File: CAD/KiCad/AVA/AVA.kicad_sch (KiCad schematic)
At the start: 9 parts, among them J1 Conn_01x40_Pin, J2 Barrel_Jack, M1 Motor_Servo, M2 Steering_Front_Servo, M3 Steering_Back_Servo, M4 Fan, SW1 SW_Push

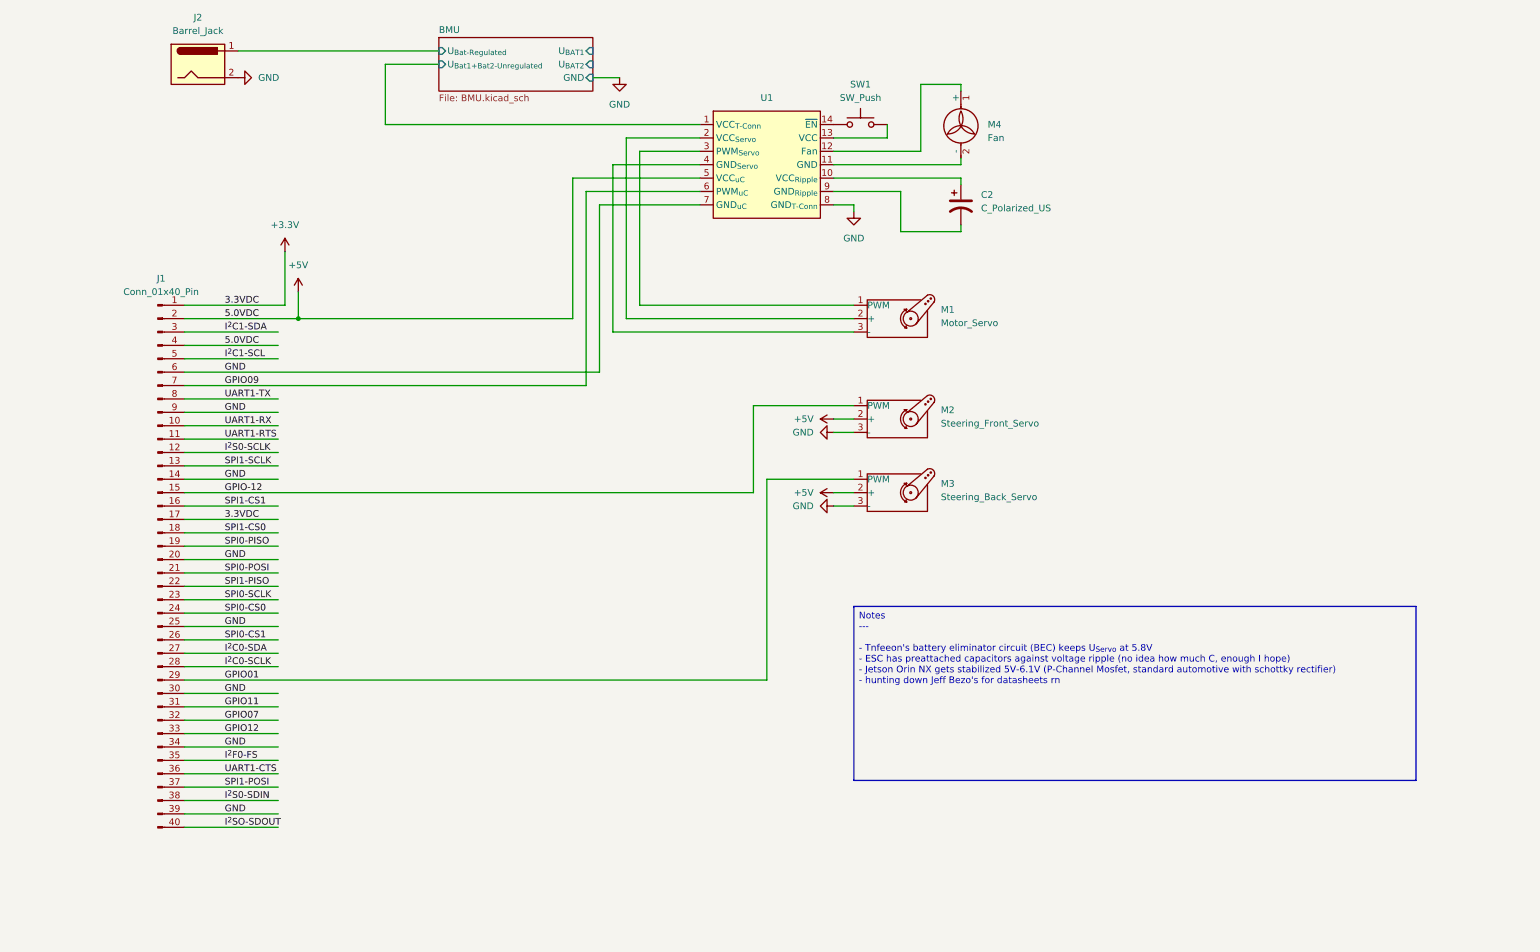
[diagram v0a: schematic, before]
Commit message: Added Graphos MBSE json file necessary for model
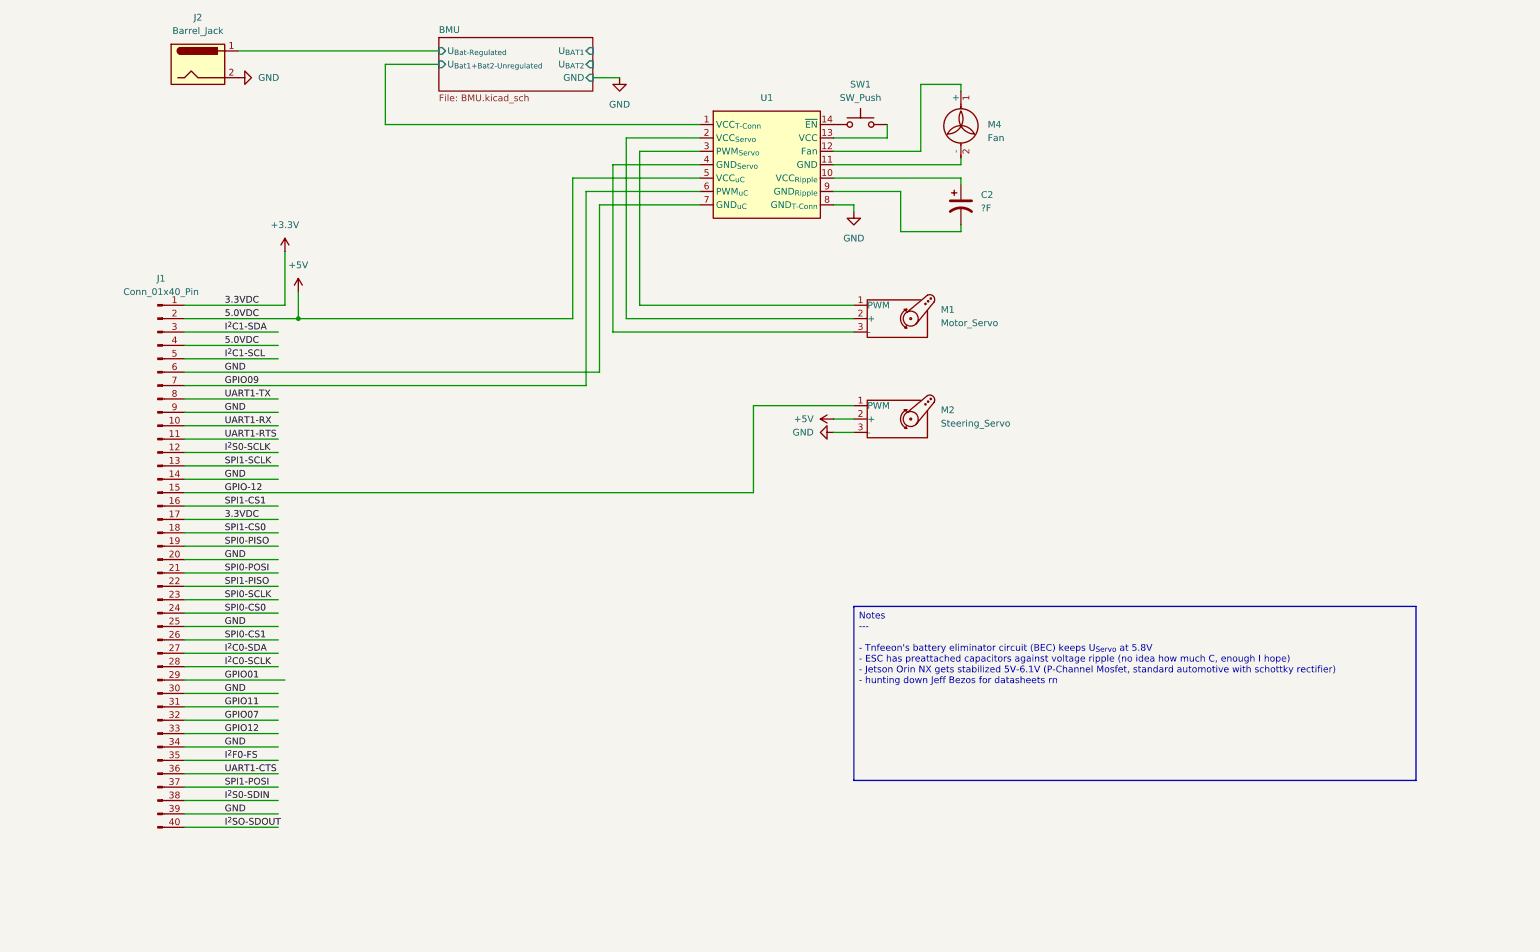
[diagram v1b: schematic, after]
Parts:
- removed M3: Steering_Back_Servo, Connector_PinHeader_2.54mm:PinHeader_1x03_P2.54mm_Vertical, symbol Motor:Motor_Servo
- C2: value C_Polarized_US -> ?F
- M2: value Steering_Front_Servo -> Steering_Servo

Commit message: ESP32-Nano for Wifi comms, ESP32-C3 for Hall Interrupt handling and BAT0, BAT1 voltage monitoring and wiring between ESC, servo and fan will be handlded on separate PCB for easier wiring. This schematic will contain this PCB, schematic and production data for it. Will probably be etched by some annoying dipshit (Meeeeeee :3)
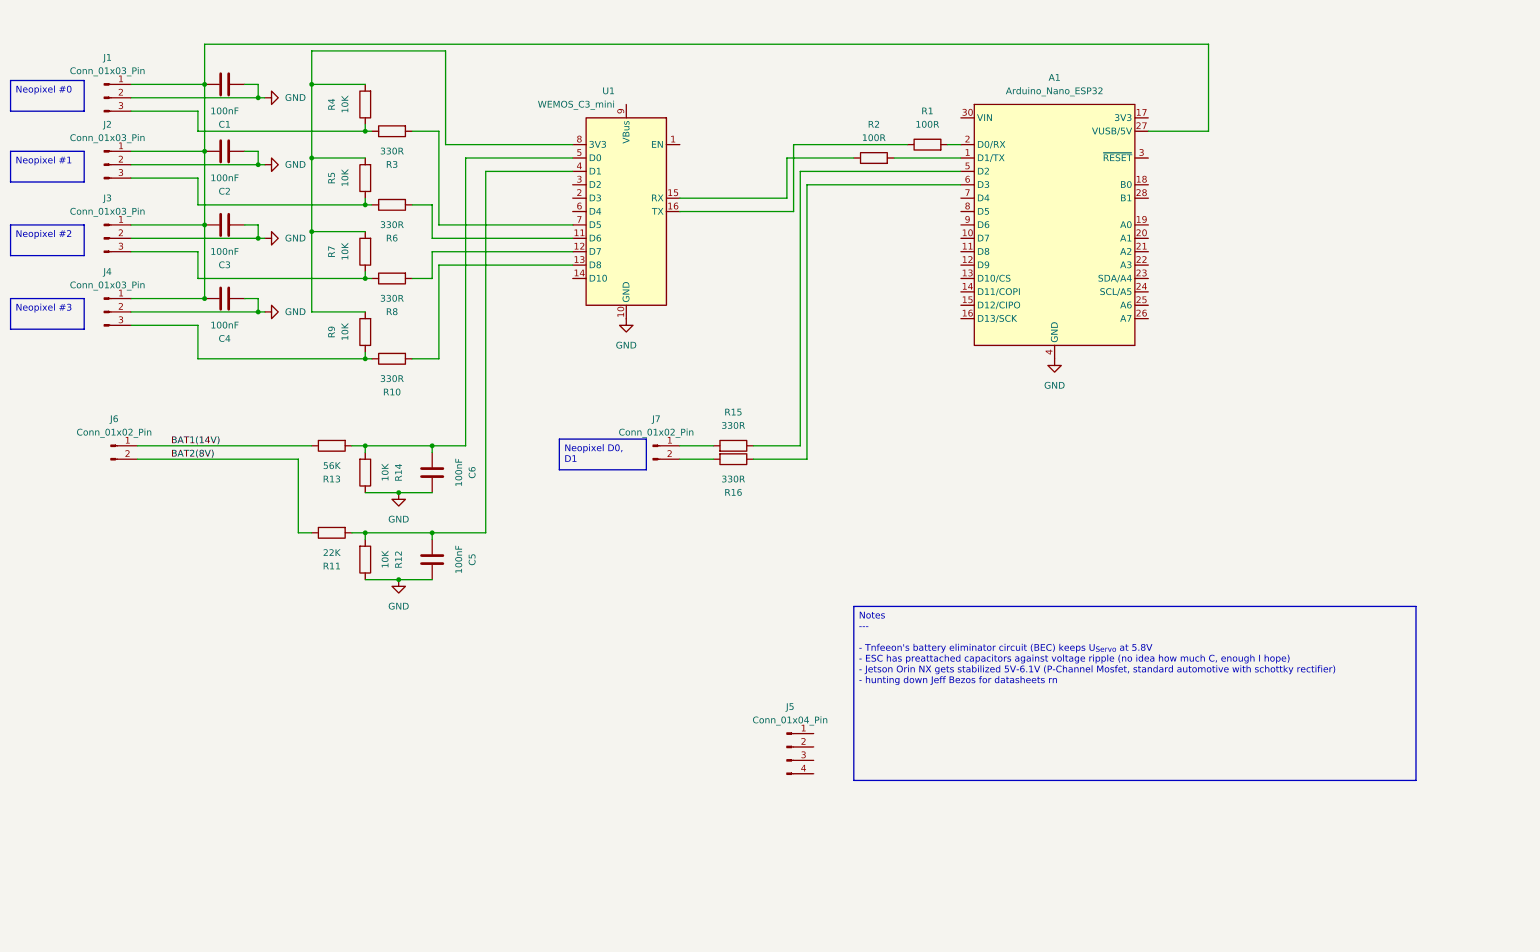
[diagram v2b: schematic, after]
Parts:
- removed C2: ?F, symbol Device:C_Polarized_US
- removed J1: Conn_01x40_Pin, Connector_PinHeader_2.54mm:PinHeader_1x40_P2.54mm_Vertical, symbol Connector:Conn_01x40_Pin
- removed J2: Barrel_Jack, Connector_BarrelJack:BarrelJack_SwitchcraftConxall_RAPC10U_Horizontal, symbol Connector:Barrel_Jack
- removed M1: Motor_Servo, Connector_PinHeader_2.54mm:PinHeader_1x03_P2.54mm_Vertical, symbol Motor:Motor_Servo
- removed M2: Steering_Servo, Connector_PinHeader_2.54mm:PinHeader_1x03_P2.54mm_Vertical, symbol Motor:Motor_Servo
- removed M4: Fan, symbol Motor:Fan
- removed SW1: SW_Push, symbol Switch:SW_Push
- removed U1: (no value), symbol AVA:ESC_Servo
- added A1: Arduino_Nano_ESP32, Module:Arduino_Nano, symbol MCU_Module:Arduino_Nano_ESP32
- added C1, C2, C3, C4, C5, C6: 100nF, Capacitor_THT:C_Disc_D5.0mm_W2.5mm_P5.00mm, symbol Device:C
- added J1, J2, J3, J4: Conn_01x03_Pin, Connector_PinSocket_2.54mm:PinSocket_1x03_P2.54mm_Vertical, symbol Connector:Conn_01x03_Pin
- added J5: Conn_01x04_Pin, symbol Connector:Conn_01x04_Pin
- added J6, J7: Conn_01x02_Pin, Connector_PinSocket_2.54mm:PinSocket_1x02_P2.54mm_Vertical, symbol Connector:Conn_01x02_Pin
- added R1, R2: 100R, Resistor_THT:R_Axial_DIN0614_L14.3mm_D5.7mm_P20.32mm_Horizontal, symbol Device:R
- added R10, R15, R16, R3, R6, R8: 330R, Resistor_THT:R_Axial_DIN0614_L14.3mm_D5.7mm_P20.32mm_Horizontal, symbol Device:R
- added R11: 22K, Resistor_THT:R_Axial_DIN0614_L14.3mm_D5.7mm_P20.32mm_Horizontal, symbol Device:R
- added R12, R14, R4, R5, R7, R9: 10K, Resistor_THT:R_Axial_DIN0614_L14.3mm_D5.7mm_P20.32mm_Horizontal, symbol Device:R
- added R13: 56K, Resistor_THT:R_Axial_DIN0614_L14.3mm_D5.7mm_P20.32mm_Horizontal, symbol Device:R
- added U1: WEMOS_C3_mini, RF_Module:WEMOS_C3_mini, symbol RF_Module:WEMOS_C3_mini
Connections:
- net GND: now also A1.29 (GND), A1.4 (GND), C1.2, C2.2, C3.2, C4.2, C5.1, C6.1, J1.2 (Pin_2), J2.2 (Pin_2), J3.2 (Pin_2), J4.2 (Pin_2), R12.1, R14.1, U1.10 (GND)
- new net: J2.3 (Pin_3), R5.1, R6.1
- new net: R6.2, U1.11 (D6)
- new net: J1.3 (Pin_3), R3.1, R4.1
- new net: R4.2, R5.2, R7.2, R9.2, U1.8 (3V3)
- new net: C6.2, R13.2, R14.2, U1.5 (D0)
- new net: A1.27 (VUSB/5V), C1.1, C2.1, C3.1, C4.1, J1.1 (Pin_1), J2.1 (Pin_1), J3.1 (Pin_1), J4.1 (Pin_1)
- new net: J4.3 (Pin_3), R10.1, R9.1
- new net: C5.2, R11.2, R12.2, U1.4 (D1)
- new net: R2.1, U1.15 (RX)
- new net: A1.1 (D1/TX), R2.2
- new net: R8.2, U1.12 (D7)
- new net: R10.2, U1.13 (D8)
- new net: R1.1, U1.16 (TX)
- new net: R3.2, U1.7 (D5)
- new net: A1.5 (D2), R15.1
- new net: J7.1 (Pin_1), R15.2
- new net: J3.3 (Pin_3), R7.1, R8.1
- new net: J7.2 (Pin_2), R16.2
- new net: A1.2 (D0/RX), R1.2
- new net: A1.6 (D3), R16.1
- new net BAT1(14V): J6.1 (Pin_1), R13.1
- new net BAT2(8V): J6.2 (Pin_2), R11.1
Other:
- removed sheet BMU

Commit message: Base connections added to schematic. Plotted PDF for others
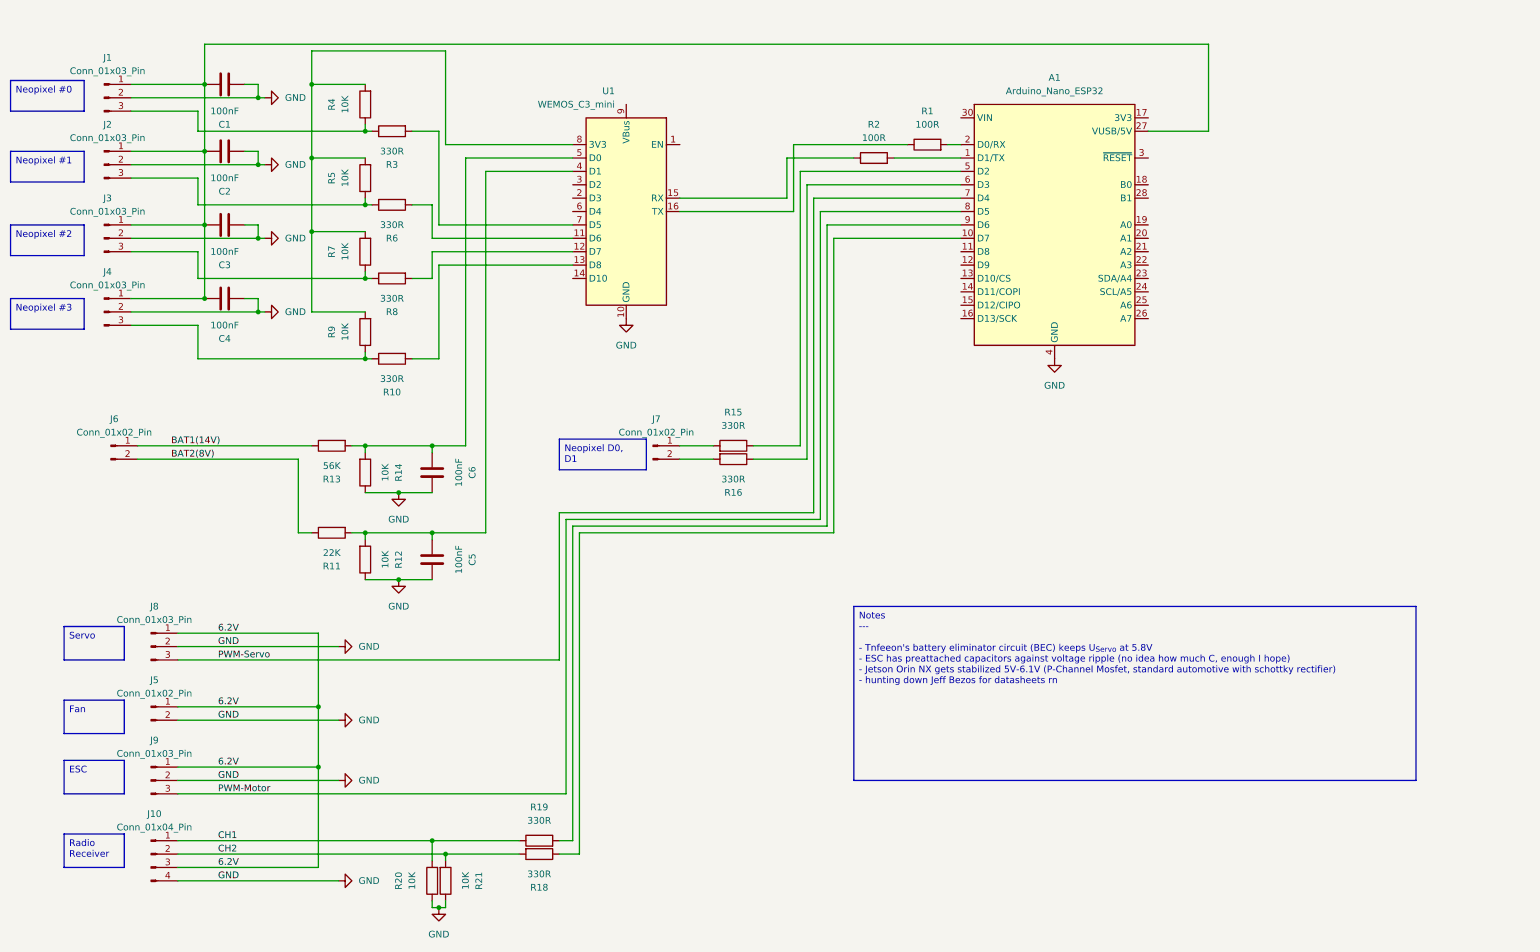
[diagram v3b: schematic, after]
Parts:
- removed J5: Conn_01x04_Pin, symbol Connector:Conn_01x04_Pin
- added J10: Conn_01x04_Pin, Connector_PinSocket_2.54mm:PinSocket_1x04_P2.54mm_Vertical, symbol Connector:Conn_01x04_Pin
- added J5: Conn_01x02_Pin, Connector_PinSocket_2.54mm:PinSocket_1x02_P2.54mm_Vertical, symbol Connector:Conn_01x02_Pin
- added J8, J9: Conn_01x03_Pin, Connector_PinSocket_2.54mm:PinSocket_1x03_P2.54mm_Vertical, symbol Connector:Conn_01x03_Pin
- added R18, R19: 330R, Resistor_THT:R_Axial_DIN0614_L14.3mm_D5.7mm_P20.32mm_Horizontal, symbol Device:R
- added R20, R21: 10K, Resistor_THT:R_Axial_DIN0614_L14.3mm_D5.7mm_P20.32mm_Horizontal, symbol Device:R
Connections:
- net GND: now also J10.4 (Pin_4), J5.2 (Pin_2), J8.2 (Pin_2), J9.2 (Pin_2), R20.1, R21.1
- net at A1.10 (D7): now also R18.1
- net PWM-Servo: now reaches A1.7 (D4)
- net PWM-Servo: now also J8.3 (Pin_3)
- net PWM-Motor: now reaches A1.8 (D5)
- net PWM-Motor: now also J9.3 (Pin_3)
- net at A1.9 (D6): now also R19.2
- new net 6.2V: J10.3 (Pin_3), J5.1 (Pin_1), J8.1 (Pin_1), J9.1 (Pin_1)
- new net CH1: J10.1 (Pin_1), R19.1, R20.2
- new net CH2: J10.2 (Pin_2), R18.2, R21.2

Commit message: Copy paste error, Hall sensors were labelled as Neopixels. Added 330R series, 10K pulldown resistor for servo-pwm, esc-pwm and neopixel D0, D1 data lines
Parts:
- added R17, R22, R25, R26: 10K, Resistor_THT:R_Axial_DIN0614_L14.3mm_D5.7mm_P20.32mm_Horizontal, symbol Device:R
- added R23, R24: 330R, Resistor_THT:R_Axial_DIN0614_L14.3mm_D5.7mm_P20.32mm_Horizontal, symbol Device:R
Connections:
- net CH1: no longer R20.2
- net CH2: no longer R21.2
- net GND: now also R17.1, R22.1, R25.1, R26.1
- net PWM-Motor: now also R23.1; no longer A1.8 (D5)
- net PWM-Servo: now also R24.1; no longer A1.7 (D4)
- net at C1.1, C2.1, C3.1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: now also U1.9 (VBus); no longer A1.27 (VUSB/5V)
- net at A1.9 (D6), R19.2: now also R21.2
- net at A1.5 (D2), R15.1: now also R17.2
- net at A1.10 (D7), R18.1: now also R20.2
- net at A1.6 (D3), R16.1: now also R22.2
- new net: A1.7 (D4), R24.2, R25.2
- new net: A1.8 (D5), R23.2, R26.2
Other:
- moved on the sheet: R20, R21

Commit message: Had to reinitialize KiCad project. Previously selected Eurocard PCB template and couldn't change back. Got normal free template now. No errors, yet
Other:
- title: Autonomous Vehicle for Alex - AVA -> (none)
